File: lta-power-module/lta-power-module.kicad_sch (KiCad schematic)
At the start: 46 parts

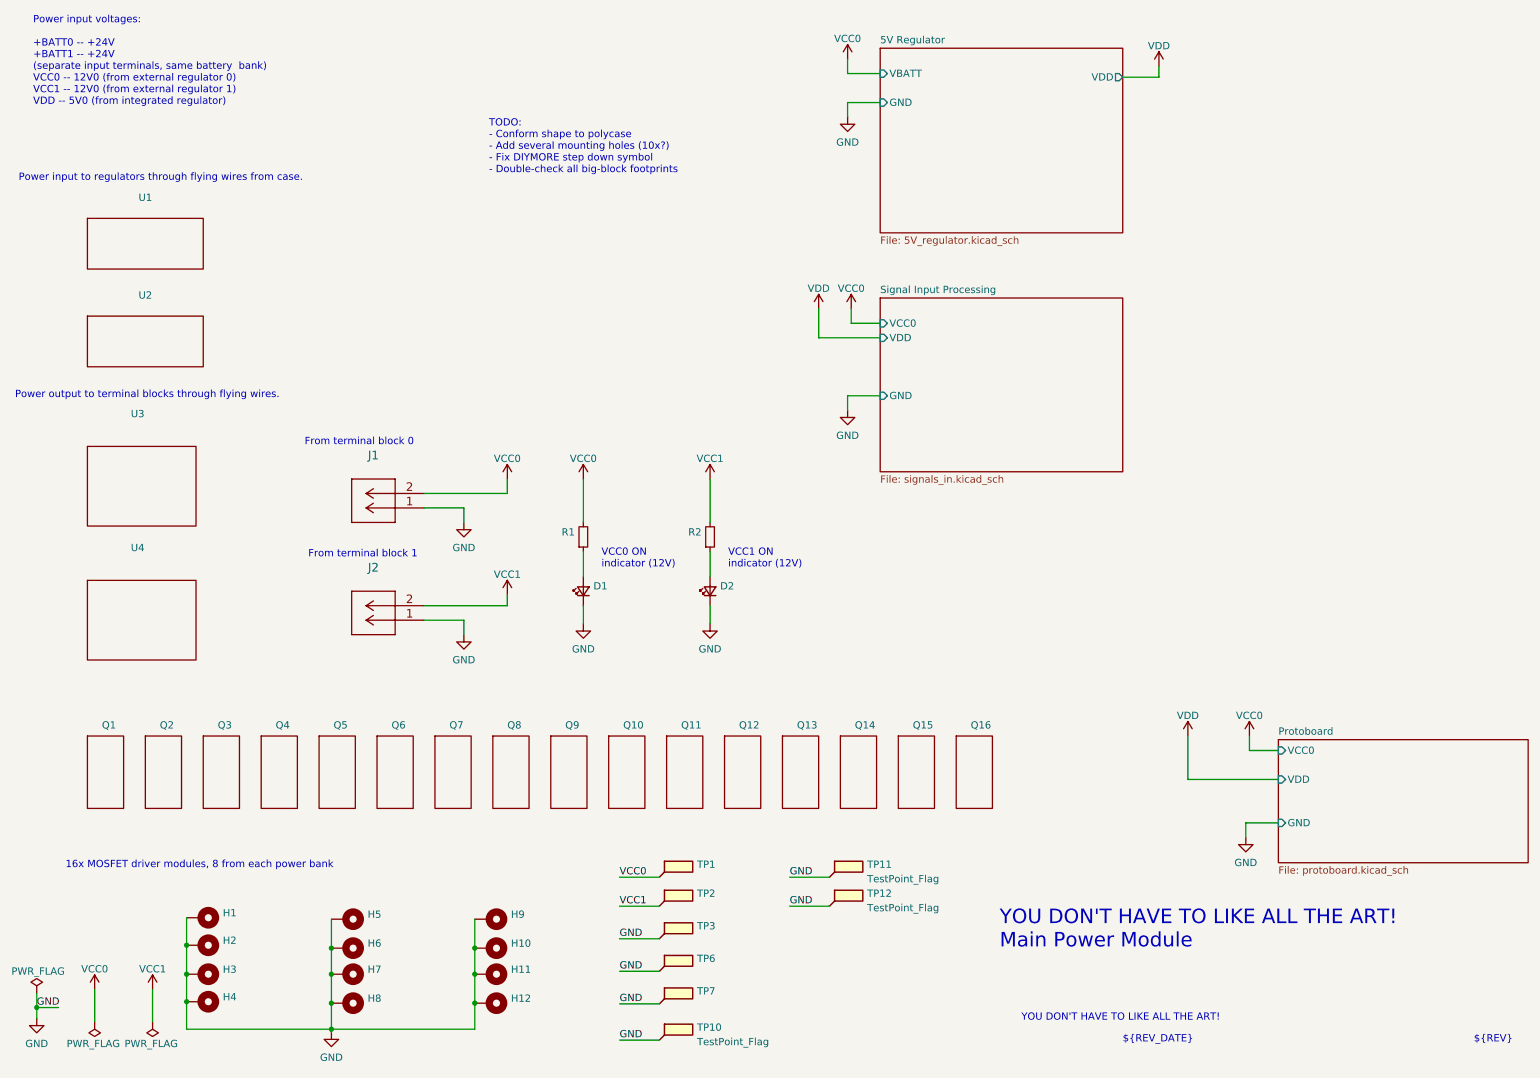
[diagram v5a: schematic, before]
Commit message: Update module footprints to be more accurate.
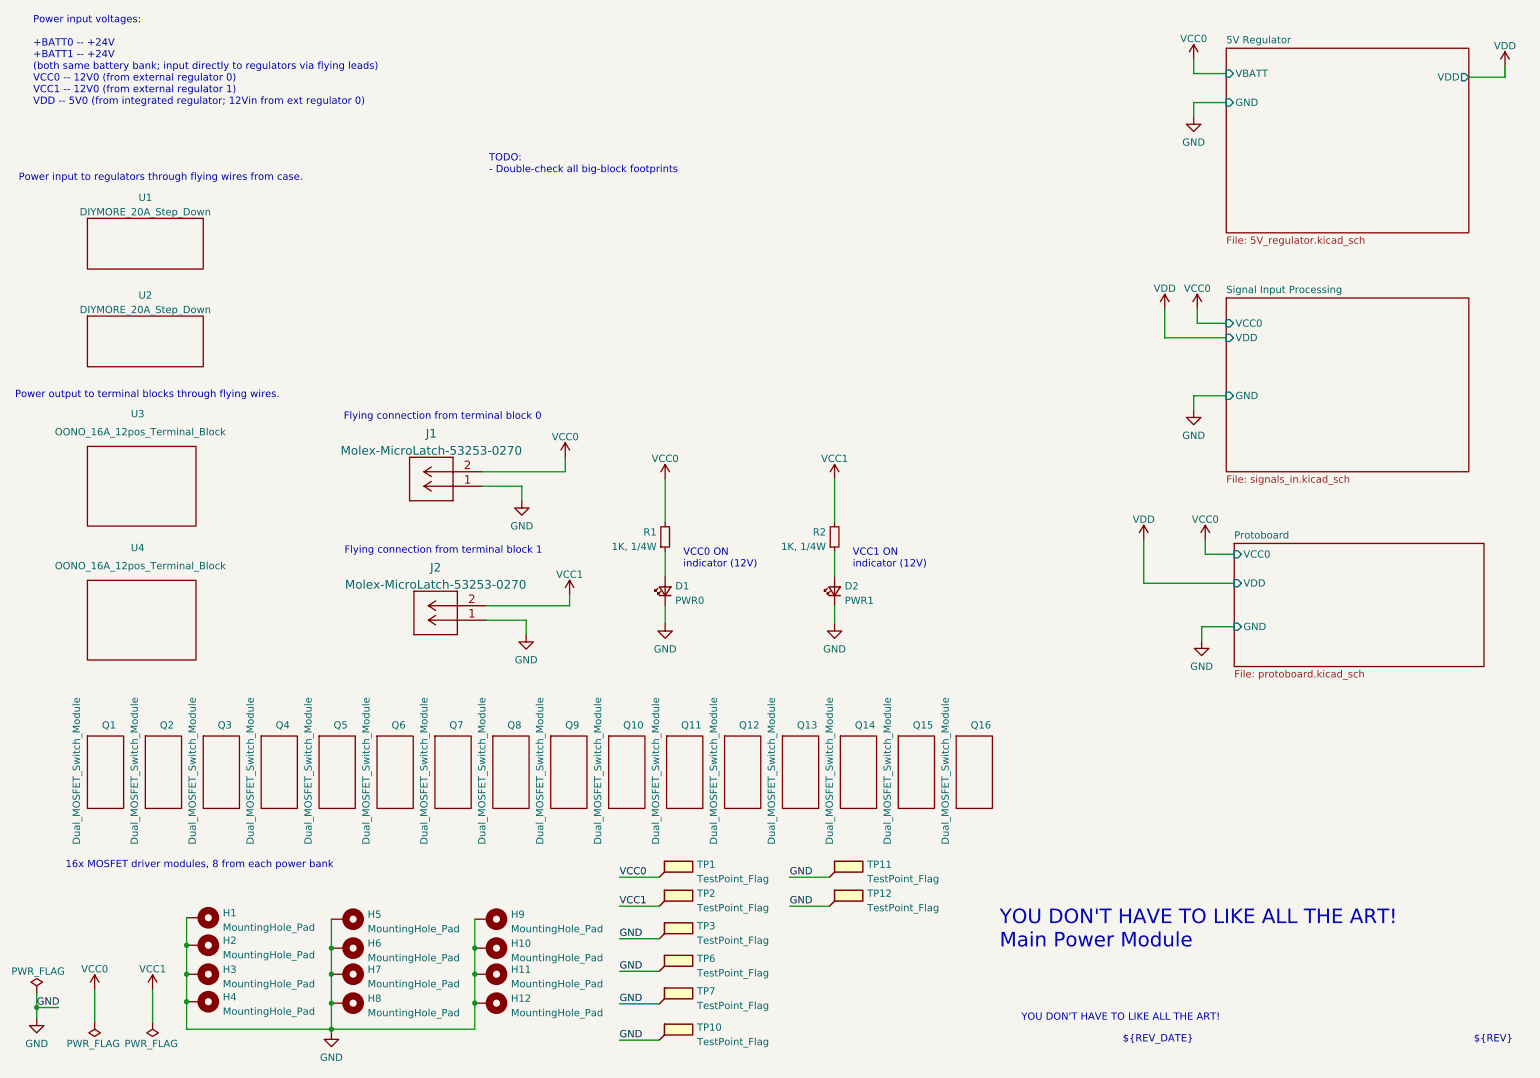
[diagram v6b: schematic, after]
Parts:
- D1: value (none) -> PWR0; footprint (none) -> Aaron_THT:LED_D5.0mm_SilkFix
- D2: value (none) -> PWR1; footprint (none) -> Aaron_THT:LED_D5.0mm_SilkFix
- H1, H10, H11, H12, H2, H3, H4, H5, H6, H7, H8, H9: value (none) -> MountingHole_Pad; footprint (none) -> MountingHole:MountingHole_5.3mm_M5_ISO7380_Pad
- J1, J2: value (none) -> Molex-MicroLatch-53253-0270; footprint (none) -> Aaron_THT:Molex-MicroLatch-53253-0270
- Q1, Q10, Q11, Q12, Q13, Q14, Q15, Q16, Q2, Q3, Q4, Q5, Q6, Q7, Q8, Q9: value (none) -> Dual_MOSFET_Switch_Module; footprint (none) -> lta-power-footprints:Dual_MOSFET_Driver
- R1, R2: value (none) -> 1K, 1/4W; footprint (none) -> Resistor_THT:R_Axial_DIN0207_L6.3mm_D2.5mm_P7.62mm_Horizontal
- TP1, TP2, TP3, TP6, TP7: value (none) -> TestPoint_Flag; footprint (none) -> Aaron_THT:TestPoint_THTPad_1.0x1.0mm_Drill0.3mm
- U1, U2: value (none) -> DIYMORE_20A_Step_Down; footprint (none) -> lta-power-footprints:12V_regulator
- U3, U4: value (none) -> OONO_16A_12pos_Terminal_Block; footprint (none) -> lta-power-footprints:12-way_power_distribution_bus; Comment (none) -> M3 screws; MANUFACTURER (none) -> OONO
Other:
- note added: "Flying connection from terminal block 0"
- note added: "Flying connection from terminal block 1"
- note added: "Power input voltages: +BATT0 -- +24V +BATT1 -- +24V (both same battery bank; input directly to regulators via flying leads) VCC0 -- 12V0 (from external regulator 0) VCC1 -- 12V0 (from external regulator 1) VDD -- 5V0 (from integrated regulator; 12Vin from ext regulator 0)"
- note added: "TODO: - Double-check all big-block footprints"
- note removed: "From terminal block 0"
- note removed: "From terminal block 1"
- note removed: "Power input voltages: +BATT0 -- +24V +BATT1 -- +24V (separate input terminals, same battery bank) VCC0 -- 12V0 (from external regulator 0) VCC1 -- 12V0 (from external regulator 1) VDD -- 5V0 (from integrated regulator)"
- note removed: "TODO: - Conform shape to polycase - Add several mounting holes (10x?) - Fix DIYMORE step down symbol - Double-check all big-block footprints"
- moved on the sheet: D1, D2, J1, J2, R1, R2

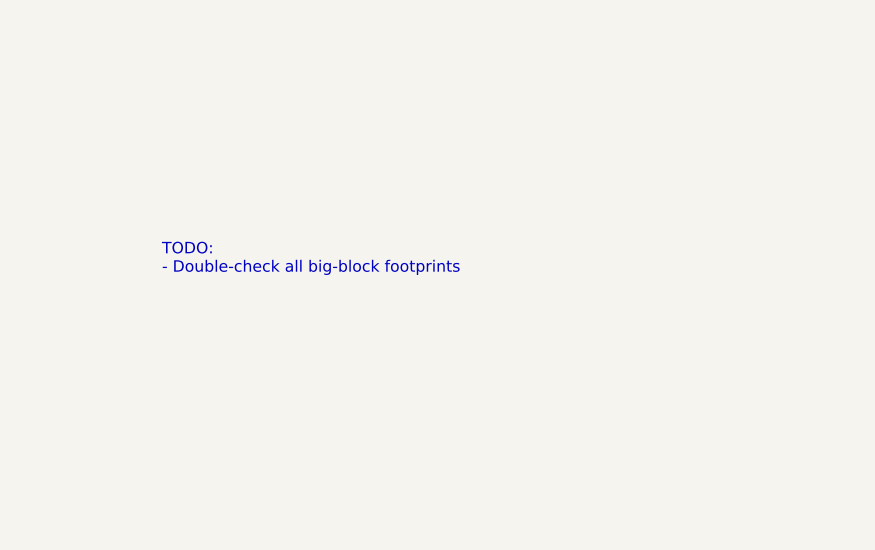
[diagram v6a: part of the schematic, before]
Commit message: Open solder masks up around mounting holes.
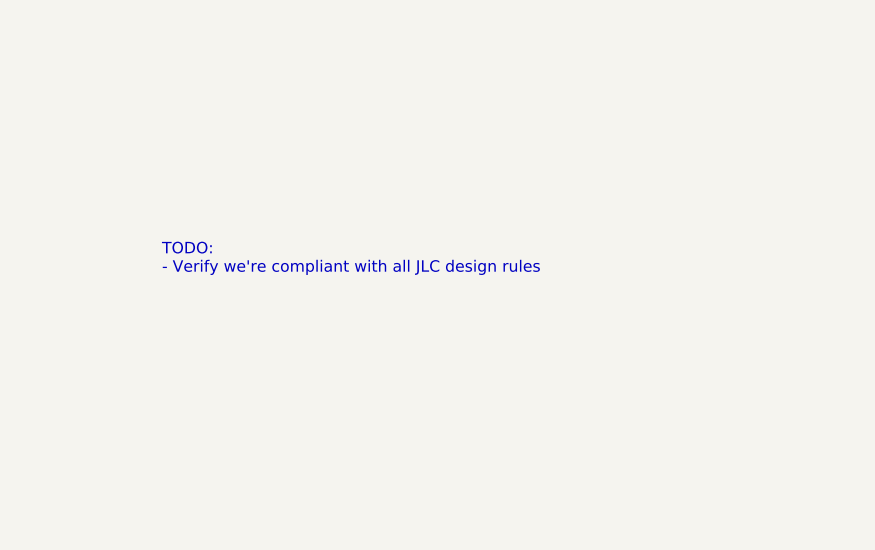
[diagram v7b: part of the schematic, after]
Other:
- note added: "TODO: - Verify we're compliant with all JLC design rules"
- note removed: "TODO: - Double-check all big-block footprints"
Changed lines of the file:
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@@
     (effects (font (size 1.27 1.27)) (justify left bottom))
   )
-  (text "TODO:\n- Double-check all big-block footprints" (at 95.8439 41.82 0)
+  (text "TODO:\n- Verify we're compliant with all JLC design rules"
+    (at 95.8439 41.82 0)
     (effects (font (size 1.27 1.27)) (justify left bottom))
   )

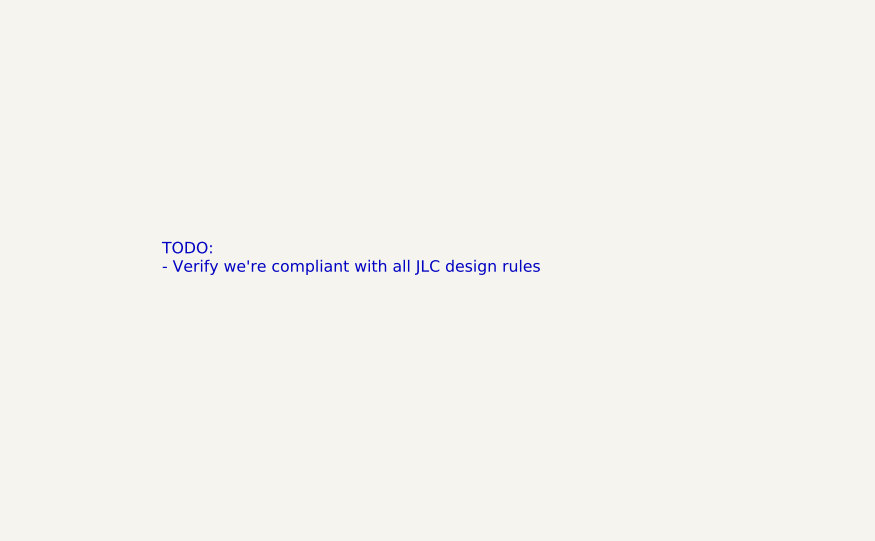
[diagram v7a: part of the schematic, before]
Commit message: Switched to plated through-holes for all mounting.
Ready for release to manufacturing.
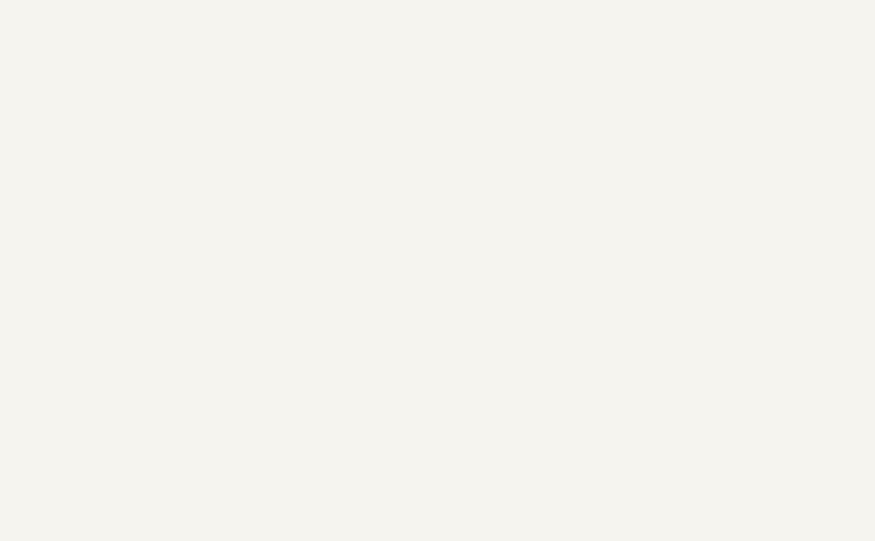
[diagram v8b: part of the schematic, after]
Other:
- note removed: "TODO: - Verify we're compliant with all JLC design rules"
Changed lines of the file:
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@@
-    (effects (font (size 1.27 1.27)) (justify left bottom))
-  )
-  (text "TODO:\n- Verify we're compliant with all JLC design rules"
-    (at 95.8439 41.82 0)
     (effects (font (size 1.27 1.27)) (justify left bottom))
   )
